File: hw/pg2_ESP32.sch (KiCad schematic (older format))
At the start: 6 parts

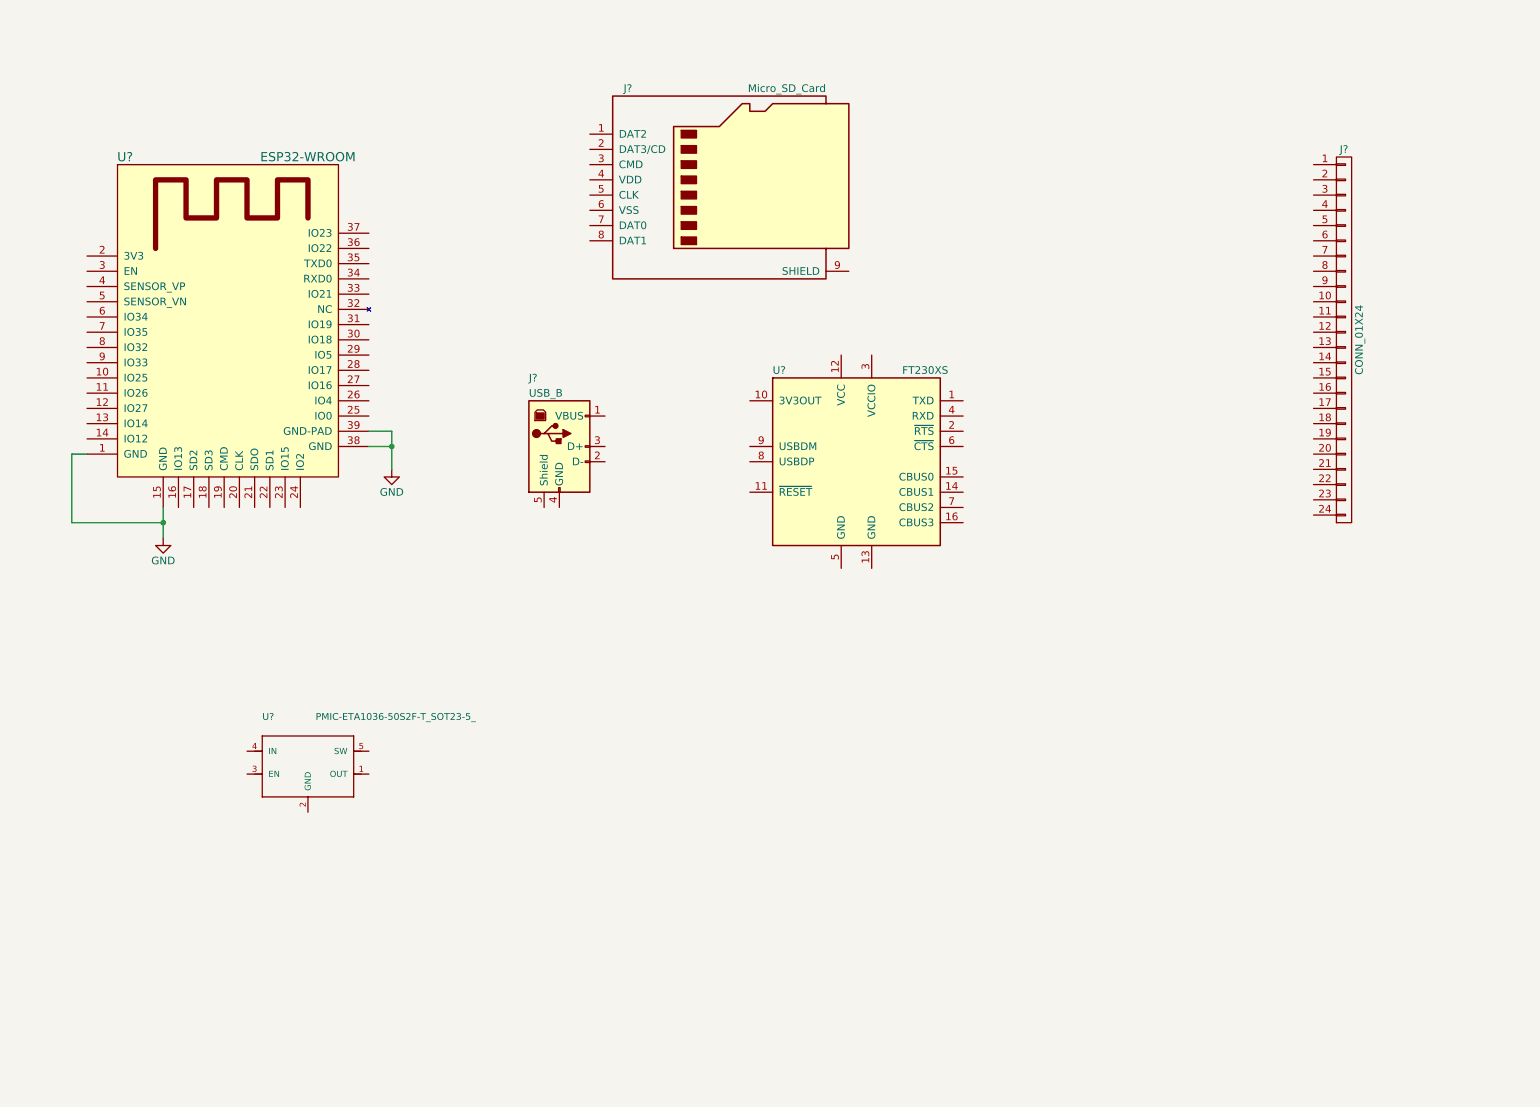
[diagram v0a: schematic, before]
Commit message: Hardware: More progress, got FTDI chip wired up
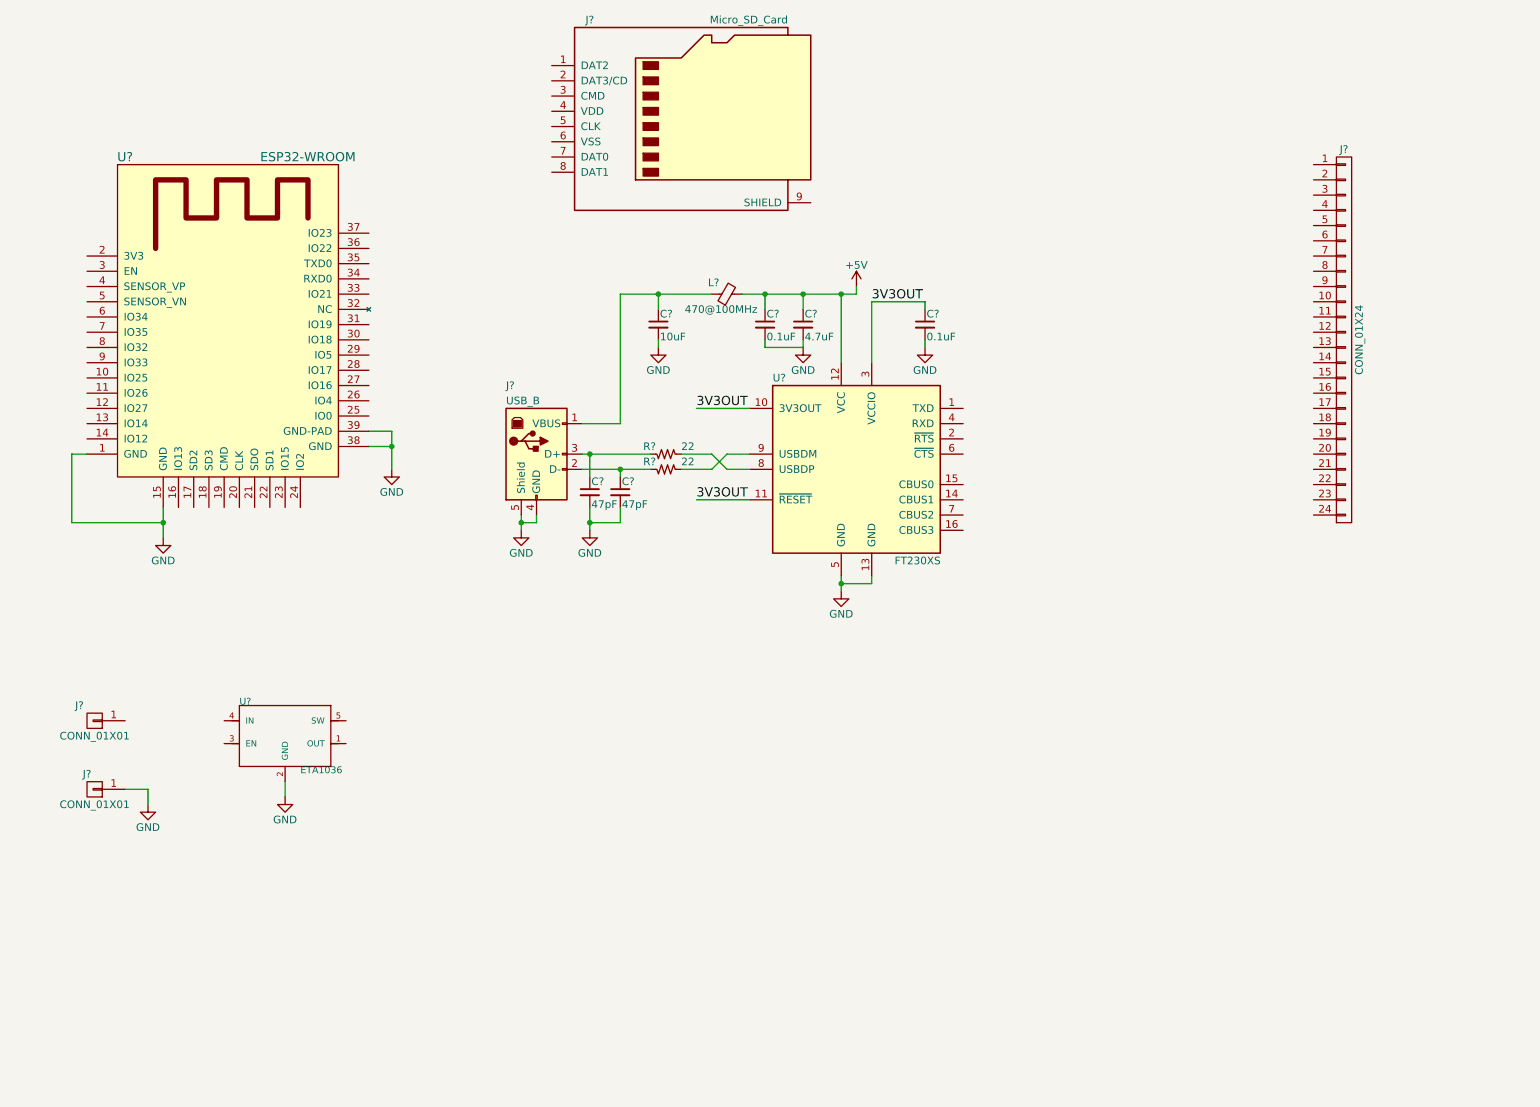
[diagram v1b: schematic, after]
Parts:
- removed U?: PMIC-ETA1036-50S2F-T_SOT23-5_, symbol PMIC-ETA1036-50S2F-T_SOT23-5_
- added C? (x2): 0.1uF, symbol C_Small
- added C?: 4.7uF, symbol C_Small
- added C?: 10uF, symbol C_Small
- added C? (x2): 47pF, symbol C_Small
- added J? (x2): CONN_01X01, symbol CONN_01X01
- added L?: 470@100MHz, symbol Ferrite_Bead_Small
- added R? (x2): 22, symbol R_Small_us
- added U?: ETA1036, symbol PMIC-ETA1036-50S2F-T_SOT23-5_
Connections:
- net GND: now also J?.4 (GND), J?.5 (Shield), U?.13 (GND), U?.5 (GND), C?.2, C?.2, C?.2, C?.2, C?.2, C?.2, J?.1 (P1), U?.2 (GND)
- net 3V3OUT: now reaches U?.10 (3V3OUT)
- net 3V3OUT: now also U?.11 (~RESET), U?.3 (VCCIO), C?.1
- net +5V: now reaches U?.12 (VCC)
- net +5V: now also C?.1, C?.1, L?.2
- net at U?.8 (USBDP): now also R?.1
- net at U?.9 (USBDM): now also R?.1
- net at J?.1 (VBUS): now also C?.1, L?.1
- net at J?.2 (D-): now also C?.1, R?.2
- net at J?.3 (D+): now also C?.1, R?.2
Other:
- moved on the sheet: J?, U?

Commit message: Hardware: Finished power supplies, SD Card, started display
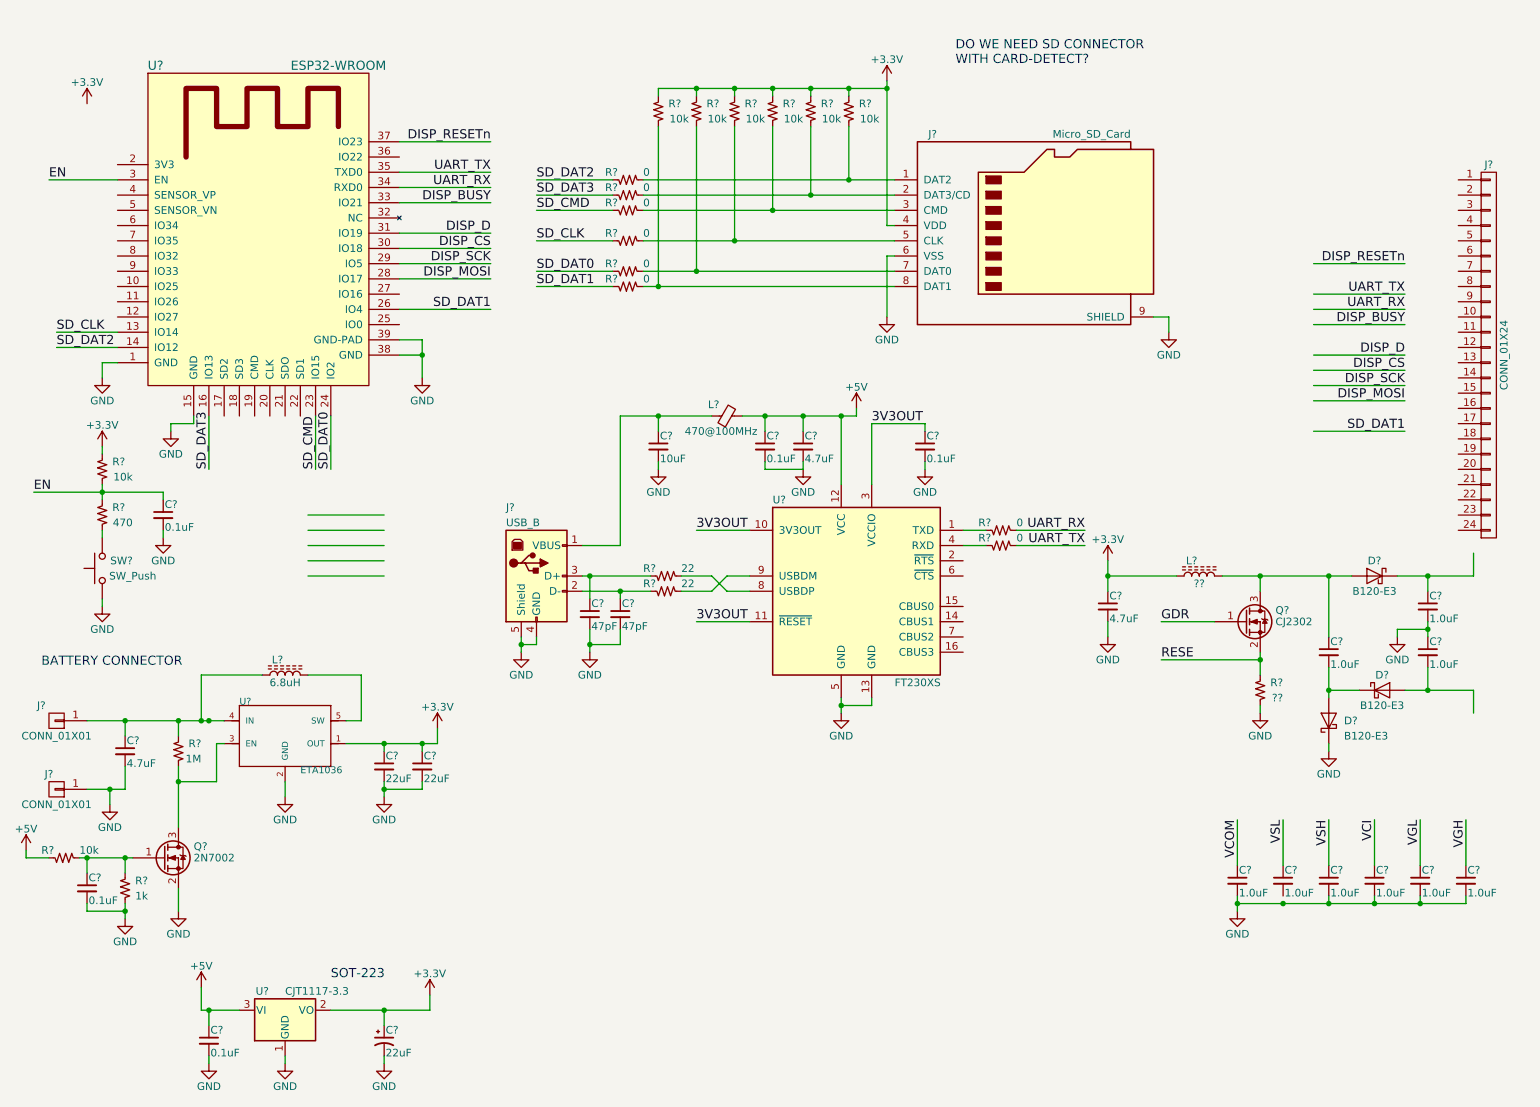
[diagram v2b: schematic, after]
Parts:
- added C? (x2): 4.7uF, symbol C_Small
- added C? (x2): 22uF, symbol C_Small
- added C?: 22uF, symbol CP1_Small
- added C? (x3): 0.1uF, symbol C_Small
- added C? (x9): 1.0uF, symbol C_Small
- added D? (x3): B120-E3, Diodes_SMD:SMA_Standard, symbol B120-E3
- added L?: 6.8uH, symbol L_Core_Ferrite
- added L?: ??, symbol L_Core_Ferrite
- added Q?: 2N7002, TO_SOT_Packages_SMD:SOT-23, symbol 2N7002
- added Q?: CJ2302, TO_SOT_Packages_SMD:SOT-23, symbol 2N7002
- added R? (x8): 0, symbol R_Small_us
- added R?: 1M, symbol R_Small_us
- added R? (x8): 10k, symbol R_Small_us
- added R?: 1k, symbol R_Small_us
- added R?: 470, symbol R_Small_us
- added R?: ??, symbol R_Small_us
- added SW?: SW_Push, symbol SW_Push
- added U?: CJT1117-3.3, symbol LT1117-3.3
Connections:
- net labels added: +3.3V, DISP_BUSY, DISP_CS, DISP_D, DISP_MOSI, DISP_RESETn, DISP_SCK, EN, GDR, RESE, SD_CLK, SD_CMD, SD_DAT0, SD_DAT1, SD_DAT2, SD_DAT3, UART_RX, UART_TX, VCI, VCOM, VGH, VGL, VSH, VSL
- wire segments 48 -> 192
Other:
- note added: "BATTERY CONNECTOR"
- note added: "DO WE NEED SD CONNECTOR \nWITH CARD-DETECT?\n"
- note added: "SOT-223"
- moved on the sheet: C?, J?, L?, R?, U?

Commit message: Hardware: Connected LCD in schematic
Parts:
- added C?: 1.0uF, symbol C_Small
- added R?: 10k, symbol R_Small_us
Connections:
- net labels added: PREVGH, PREVGL, VBATT
- wire segments 192 -> 215
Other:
- moved on the sheet: J?
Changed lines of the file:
@@
 L CONN_01X24 J?
 U 1 1 598E3FC6
-P 10200 2800
-F 0 "J?" H 10200 4050 50  0000 C CNN
-F 1 "CONN_01X24" V 10300 2800 50  0000 C CNN
-F 2 "" H 10200 2800 50  0001 C CNN
-F 3 "" H 10200 2800 50  0001 C CNN
-	1    10200 2800
-	1    0    0    -1
+P 10150 2600
+F 0 "J?" H 10150 3850 50  0000 C CNN
+F 1 "CONN_01X24" V 10250 2600 50  0000 C CNN
+F 2 "" H 10150 2600 50  0001 C CNN
+F 3 "" H 10150 2600 50  0001 C CNN
+	1    10150 2600
+	1    0    0    1
 $EndComp
 $Comp
@@
 L +3.3V #PWR?
 U 1 1 59930507
-P 1000 1150
-F 0 "#PWR?" H 1000 1000 50  0001 C CNN
-F 1 "+3.3V" H 1000 1290 50  0000 C CNN
-F 2 "" H 1000 1150 50  0001 C CNN
-F 3 "" H 1000 1150 50  0001 C CNN
-	1    1000 1150
+P 1150 1050
+F 0 "#PWR?" H 1150 900 50  0001 C CNN
+F 1 "+3.3V" H 1150 1190 50  0000 C CNN
+F 2 "" H 1150 1050 50  0001 C CNN
+F 3 "" H 1150 1050 50  0001 C CNN
+	1    1150 1050
 	1    0    0    -1
 $EndComp
@@
 Text Label 3950 2350 0    60   ~ 0
 SD_DAT1
-Wire Wire Line
-	2950 3850 2450 3850
-Wire Wire Line
-	2950 3950 2450 3950
-Wire Wire Line
-	2950 4050 2450 4050
-Wire Wire Line
-	2950 4150 2450 4150
-Wire Wire Line
-	2950 4250 2450 4250
 Text Label 800  2750 0    60   ~ 0
 SD_DAT2
@@
 Text Label 3650 2300 2    60   ~ 0
 DISP_MOSI
-Wire Wire Line
-	9050 2500 9650 2500
-Wire Wire Line
-	9050 2400 9650 2400
-Text Label 9650 2500 2    60   ~ 0
-UART_RX
-Text Label 9650 2400 2    60   ~ 0
-UART_TX
-Text Label 9650 3300 2    60   ~ 0
-SD_DAT1
-Wire Wire Line
-	9050 3300 9650 3300
-Wire Wire Line
-	9050 2200 9650 2200
-Text Label 9650 2200 2    60   ~ 0
-DISP_RESETn
-Wire Wire Line
-	9050 2600 9650 2600
-Text Label 9650 2600 2    60   ~ 0
-DISP_BUSY
-Wire Wire Line
-	9050 2800 9650 2800
-Text Label 9650 2800 2    60   ~ 0
-DISP_D
-Wire Wire Line
-	9050 2900 9650 2900
-Wire Wire Line
-	9050 3000 9650 3000
-Wire Wire Line
-	9050 3100 9650 3100
-Text Label 9650 2900 2    60   ~ 0
-DISP_CS
-Text Label 9650 3000 2    60   ~ 0
-DISP_SCK
-Text Label 9650 3100 2    60   ~ 0
-DISP_MOSI
 $Comp
 L 2N7002 Q?
@@
 Wire Wire Line
 	9800 4850 9800 5000
+Wire Wire Line
+	10100 4100 10450 4100
+Text Label 10450 4100 2    60   ~ 0
+PREVGH
+Wire Wire Line
+	10100 5150 10450 5150
+Text Label 10450 5150 2    60   ~ 0
+PREVGL
+Wire Wire Line
+	9950 3750 9400 3750
+Wire Wire Line
+	9950 3650 9400 3650
+Wire Wire Line
+	9950 3550 9400 3550
+Wire Wire Line
+	9950 3450 9400 3450
+Wire Wire Line
+	9950 3350 9400 3350
+Wire Wire Line
+	9950 3250 9400 3250
+Wire Wire Line
+	9250 3050 9950 3050
+Wire Wire Line
+	9950 2950 9850 2950
+Wire Wire Line
+	9250 2850 9950 2850
+Wire Wire Line
+	9950 2750 9400 2750
+Wire Wire Line
+	9950 2650 9400 2650
+Wire Wire Line
+	9950 2550 9400 2550
+Wire Wire Line
+	9950 2450 9400 2450
+Wire Wire Line
+	9950 2350 9400 2350
+Wire Wire Line
+	9950 2250 9400 2250
+Wire Wire Line
+	9250 2150 9950 2150
+Wire Wire Line
+	9950 2050 9400 2050
+Wire Wire Line
+	9950 1950 9400 1950
+Wire Wire Line
+	9950 1850 9400 1850
+Wire Wire Line
+	9950 1750 9400 1750
+Wire Wire Line
+	9950 1650 9400 1650
+Wire Wire Line
+	9950 1550 9400 1550
+Wire Wire Line
+	9950 1450 9400 1450
+Text Label 9400 3750 0    60   ~ 0
+VCOM
+Text Label 9400 3650 0    60   ~ 0
+PREVGL
+Text Label 9400 3550 0    60   ~ 0
+VSL
+Text Label 9400 3450 0    60   ~ 0
+PREVGH
+Text Label 9400 3350 0    60   ~ 0
+VSH
+$Comp
+L GND #PWR?
+U 1 1 5993DD64
+P 9250 3150
+F 0 "#PWR?" H 9250 2900 50  0001 C CNN
+F 1 "GND" H 9250 3000 50  0000 C CNN
+F 2 "" H 9250 3150 50  0001 C CNN
+F 3 "" H 9250 3150 50  0001 C CNN
+	1    9250 3150
+	1    0    0    -1
+$EndComp
+Wire Wire Line
+	9250 3050 9250 3150
+Wire Wire Line
+	9850 2850 9850 3150
+Connection ~ 9850 2950
+Connection ~ 9850 2850
+Wire Wire Line
+	9850 3150 9950 3150
+Wire Wire Line
+	9250 2850 9250 2750
+$Comp
+L +3.3V #PWR?
+U 1 1 5993E9CB
+P 9250 2750
+F 0 "#PWR?" H 9250 2600 50  0001 C CNN
+F 1 "+3.3V" H 9250 2890 50  0000 C CNN
+F 2 "" H 9250 2750 50  0001 C CNN
+F 3 "" H 9250 2750 50  0001 C CNN
+	1    9250 2750
+	1    0    0    -1
+$EndComp
+$Comp
+L GND #PWR?
+U 1 1 5993ED09
+P 9250 2250
+F 0 "#PWR?" H 9250 2000 50  0001 C CNN
+F 1 "GND" H 9250 2100 50  0000 C CNN
+F 2 "" H 9250 2250 50  0001 C CNN
+F 3 "" H 9250 2250 50  0001 C CNN
+	1    9250 2250
+	1    0    0    -1
+$EndComp
+Wire Wire Line
+	9250 2150 9250 2250
+Text Label 9400 1750 0    60   ~ 0
+VGL
+Text Label 9400 1850 0    60   ~ 0
+VGH
+Text Label 9400 1550 0    60   ~ 0
+GDR
+Text Label 9400 1650 0    60   ~ 0
+RESE
+Text Label 9400 2250 0    60   ~ 0
+DISP_BUSY
+Text Label 9400 2350 0    60   ~ 0
+DISP_RESETn
+Text Label 9400 2450 0    60   ~ 0
+DISP_D
+Text Label 9400 2550 0    60   ~ 0
+DISP_CS
+Text Label 9400 2650 0    60   ~ 0
+DISP_SCK
+Text Label 9400 2750 0    60   ~ 0
+DISP_MOSI
+Wire Wire Line
+	1150 1550 1200 1550
+Wire Wire Line
+	1150 1050 1150 1550
+$Comp
+L C_Small C?
+U 1 1 599446B2
+P 900 1250
+F 0 "C?" H 910 1320 50  0000 L CNN
+F 1 "1.0uF" H 910 1170 50  0000 L CNN
+F 2 "" H 900 1250 50  0001 C CNN
+F 3 "" H 900 1250 50  0001 C CNN
+F 4 "302010139" H 900 1250 60  0001 C CNN "SKU"
+	1    900  1250
+	1    0    0    -1
+$EndComp
+Wire Wire Line
+	1150 1100 900  1100
+Wire Wire Line
+	900  1100 900  1150
+Connection ~ 1150 1100
+$Comp
+L GND #PWR?
+U 1 1 5994539A
+P 900 1400
+F 0 "#PWR?" H 900 1150 50  0001 C CNN
+F 1 "GND" H 900 1250 50  0000 C CNN
+F 2 "" H 900 1400 50  0001 C CNN
+F 3 "" H 900 1400 50  0001 C CNN
+	1    900  1400
+	1    0    0    -1
+$EndComp
+Wire Wire Line
+	900  1350 900  1400
+Text Label 1000 5200 0    60   ~ 0
+VBATT
+Text Label 2750 3750 0    60   ~ 0
+VBATT
+Wire Wire Line
+	2750 3750 3100 3750
+Wire Wire Line
+	3100 3750 3100 3800
+$Comp
+L R_Small_us R?
+U 1 1 59947780
+P 3100 3900
+F 0 "R?" H 2950 3850 50  0000 L CNN
+F 1 "10k" H 2900 3950 50  0000 L CNN
+F 2 "" H 3100 3900 50  0001 C CNN
+F 3 "" H 3100 3900 50  0001 C CNN
+F 4 "301010293" V 3100 3900 60  0001 C CNN "SKU"
+	1    3100 3900
+	-1   0    0    1
+$EndComp
 $EndSCHEMATC

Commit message: hw: cleaned up part numbers, exported initial BOM
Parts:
- removed J? (x2): CONN_01X01, symbol CONN_01X01
- added BT1: Battery_Cell, Battery_Holders:Keystone_2466_1xAAA, symbol Battery_Cell
- added TP1, TP10, TP11, TP12, TP13, TP14, TP15, TP2, TP3, TP4, TP5, TP6, TP7, TP8, TP9: TEST_POINT, Wire_Pads:SolderWirePad_single_0-8mmDrill, symbol CONN_01X01
- C1, C10, C12, C14, C16, C17, C18, C19, C2, C20, C21, C22, C23, C24, C4, C5, C9: renamed from C?; footprint (none) -> Capacitors_SMD:C_0603
- C11: renamed from C?; footprint (none) -> Capacitors_SMD:C_0603; SKU (none) -> 302010103
- C13, C15, C3: renamed from C?; footprint (none) -> Capacitors_SMD:C_0603; SKU (none) -> 302010111
- C6, C8: renamed from C?; footprint (none) -> Capacitors_SMD:C_0805
- C7: renamed from C?; footprint (none) -> Capacitors_Tantalum_SMD:CP_Tantalum_Case-A_EIA-3216-18_Reflow
- D1, D2, D3: renamed from D?; value B120-E3 -> B540; SKU (none) -> 304020012
- J5: renamed from J?; SKU (none) -> 320060000
- L1: renamed from L?; value 6.8uH -> 10uH; footprint (none) -> Inductors_SMD:L_Taiyo-Yuden_NR-60xx_HandSoldering; SKU SWPA4030S6R8MT -> 303010016
- L2: renamed from L?; footprint (none) -> Inductors_SMD:L_0805
- L3: renamed from L?; value ?? -> 22uH; footprint (none) -> Inductors_SMD:L_Taiyo-Yuden_NR-40xx_HandSoldering; SKU aoue -> 303010702
- R1, R15, R16, R17, R18, R19, R2, R20, R3, R4, R5, R6, R7: renamed from R?; footprint (none) -> Resistors_SMD:R_0603
- R10, R12, R14, R22: renamed from R?; footprint (none) -> Resistors_SMD:R_0603; SKU 22 -> 301010292
- R11, R13, R21, R9: renamed from R?; footprint (none) -> Resistors_SMD:R_0603; SKU 301010289 -> 301010292
- R8: renamed from R?; footprint (none) -> Resistors_SMD:R_0603; SKU 22 -> 301010289
- SW1: renamed from SW?; footprint (none) -> Buttons_Switches_SMD:SW_SPST_SKQG
- U1: renamed from U?; MPN (none) -> ESP32-WROOM-32
- U2: renamed from U?; value ETA1036 -> ETA1036-33S2F-T; footprint (none) -> TO_SOT_Packages_SMD:SOT-23-5; MPN ETA1036-50S2F-T -> ETA1036-33S2F-T; SKU 310030153 -> (none)
- U3: renamed from U?; footprint (none) -> TO_SOT_Packages_SMD:SOT-223-3_TabPin2
- U4: renamed from U?; footprint SSOP-16 -> Housings_SSOP:SSOP-16_3.9x4.9mm_Pitch0.635mm
- gave numbers to parts that had none: 5
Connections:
- net 3V3OUT: now also TP2.1 (P1)
- net GND: now also BT1.2 (-)
- net PREVGH: now also TP14.1 (P1)
- net PREVGL: now also TP15.1 (P1)
- net RESE: now also TP9.1 (P1)
- net VBATT: now also BT1.1 (+)
- net at J5.18 (P18): now also TP12.1 (P1)
- net at J5.19 (P19): now also TP11.1 (P1)
- net at J5.24 (P24): now also TP10.1 (P1)
- net at J5.6 (P6): now also TP13.1 (P1)
- net at U4.14 (CBUS1): now also TP6.1 (P1)
- net at U4.15 (CBUS0): now also TP5.1 (P1)
- net at U4.16 (CBUS3): now also TP8.1 (P1)
- net at U4.2 (~RTS): now also TP3.1 (P1)
- net at U4.6 (~CTS): now also TP4.1 (P1)
- net at U4.7 (CBUS2): now also TP7.1 (P1)
- net at Q1.3 (D), R5.1, U2.3 (EN): now also TP1.1 (P1)
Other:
- moved on the sheet: C6, C8, J4, R10, R11, R12, R13, R14, R15, R16, R17, R18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
